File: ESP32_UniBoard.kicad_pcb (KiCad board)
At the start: 2 copper layers, 30 x 43.8 mm, 21 parts, among them J1 USB_C_Receptacle_USB2.0, J2 Conn_01x06_Socket, J3 Hirose DF40C, SW1 SW_Push, SW2 SW_Push, U1 ESP32-S3-WROOM-1, U2 SPX3819M5-L-3-3

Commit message: Schematics and PCB updates
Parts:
- added C9: 100nF, Capacitor_SMD:C_0603_1608Metric_Pad1.08x0.95mm_HandSolder, F.Cu at (116.7, 79.8)
- added D3: RED, LED_SMD:LED_0603_1608Metric_Pad1.05x0.95mm_HandSolder, F.Cu at (132.6, 77.7)
- added D4: YL, LED_SMD:LED_0603_1608Metric_Pad1.05x0.95mm_HandSolder, F.Cu at (134.6, 77.7)
- added F1: Polyfuse, Fuse:Fuse_1206_3216Metric_Pad1.42x1.75mm_HandSolder, F.Cu at (117.0, 82.9)
- added R5: R, Resistor_SMD:R_0603_1608Metric_Pad0.98x0.95mm_HandSolder, F.Cu at (132.6, 74.3)
- added R6: R, Resistor_SMD:R_0603_1608Metric_Pad0.98x0.95mm_HandSolder, F.Cu at (134.6, 74.3)
- added U3: USBLC6-2SC6, Package_TO_SOT_SMD:SOT-23-6, F.Cu at (117.1, 77.3)
- D2: renamed from D1; value LED -> GRN
- moved J3 13.9 mm to (121.3, 74.1), turned to 0 degrees
- moved R1 10.7 mm to (108.6, 84.4), turned to 180 degrees
- moved R2 4.93 mm to (112.1, 84.4), turned to 0 degrees
- moved C8 4.80 mm to (122.7, 81.0), turned to -90 degrees
- moved C6 4.52 mm to (124.8, 76.8)
- moved U2 4.39 mm to (125.7, 81.0)
- moved C7 4.30 mm to (125.9, 83.5)
- moved D2 3.52 mm to (130.5, 77.7)
- moved R4 3.41 mm to (130.5, 74.3)
- moved D1 2.87 mm to (121.0, 81.0)
- moved C1 1.80 mm to (108.2, 60.6)
- moved R3 1.77 mm to (108.2, 57.3)
- moved C2 0.21 mm to (133.0, 90.7)
- moved C5 0.21 mm to (110.4, 90.7)
- moved SW1 0.21 mm to (126.9, 90.7)
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- renumbered D2 to D1
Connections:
- D1 pad 2: Net-(D2-A) (its old number) -> Net-(D1-A)
- J1 pad A4: Net-(D2-A) (its old number) -> VBUS
- J1 pad A9: Net-(D2-A) (its old number) -> VBUS
- J1 pad B4: Net-(D2-A) (its old number) -> VBUS
- J1 pad B9: Net-(D2-A) (its old number) -> VBUS
- J3 pad 10: /GPIO17 -> /GPIO6
- J3 pad 11: /GPIO18 -> /GPIO5
- J3 pad 12: /GPIO8 -> /GPIO4
- J3 pad 14: /USB_D_N -> /GPIO1
- J3 pad 15: /USB_D_P -> /GPIO2
- J3 pad 16: /GPIO3 -> /ESP_TX
- J3 pad 17: /GPIO46 -> /ESP_RX
- J3 pad 19: /GPIO9 -> /GPIO42
- J3 pad 20: /GPIO10 -> /GPIO41
- J3 pad 21: /GPIO11 -> /GPIO40
- J3 pad 22: /GPIO12 -> /GPIO39
- J3 pad 23: /GPIO13 -> /GPIO38
- J3 pad 28: /GPIO14 -> unconnected-(J3-Pin_28-Pad28)
- J3 pad 29: /GPIO21 -> unconnected-(J3-Pin_29-Pad29)
- J3 pad 3: /GPIO4 -> /GPIO8
- J3 pad 30: /GPIO47 -> unconnected-(J3-Pin_30-Pad30)
- J3 pad 31: /GPIO48 -> unconnected-(J3-Pin_31-Pad31)
- J3 pad 32: /GPIO45 -> unconnected-(J3-Pin_32-Pad32)
- J3 pad 34: /BOOT -> unconnected-(J3-Pin_34-Pad34)
- J3 pad 35: /GPIO35 -> unconnected-(J3-Pin_35-Pad35)
- J3 pad 36: /GPIO36 -> unconnected-(J3-Pin_36-Pad36)
- J3 pad 37: /GPIO37 -> unconnected-(J3-Pin_37-Pad37)
- J3 pad 39: /GPIO38 -> unconnected-(J3-Pin_39-Pad39)
- J3 pad 4: /GPIO5 -> /GPIO18
- J3 pad 40: /GPIO39 -> /GPIO12
- J3 pad 41: /GPIO40 -> /GPIO11
- J3 pad 42: /GPIO41 -> /GPIO10
- J3 pad 44: /GPIO42 -> /GPIO9
- J3 pad 45: /ESP_RX -> /GPIO46
- J3 pad 46: /ESP_TX -> /GPIO3
- J3 pad 47: /GPIO2 -> /USB_D_N
- J3 pad 48: /GPIO1 -> /USB_D_P
- J3 pad 5: /GPIO6 -> /GPIO17
- J3 pad 6: /GPIO7 -> /GPIO16
- J3 pad 9: /GPIO16 -> /GPIO7
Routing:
- net /EN: track 7.25 -> 0.00 mm
- net +5V: track 7.24 -> 0.00 mm
- net Net-(J1-CC2): track 2.27 -> 0.00 mm
- net Net-(J1-CC1): track 2.16 -> 0.00 mm
- net +3V3: track 10.8 -> 8.66 mm
- net GND: track 3.16 -> 1.74 mm
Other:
- board text added: "IO35"
- board text added: "PWR"
- board text added: "RX"

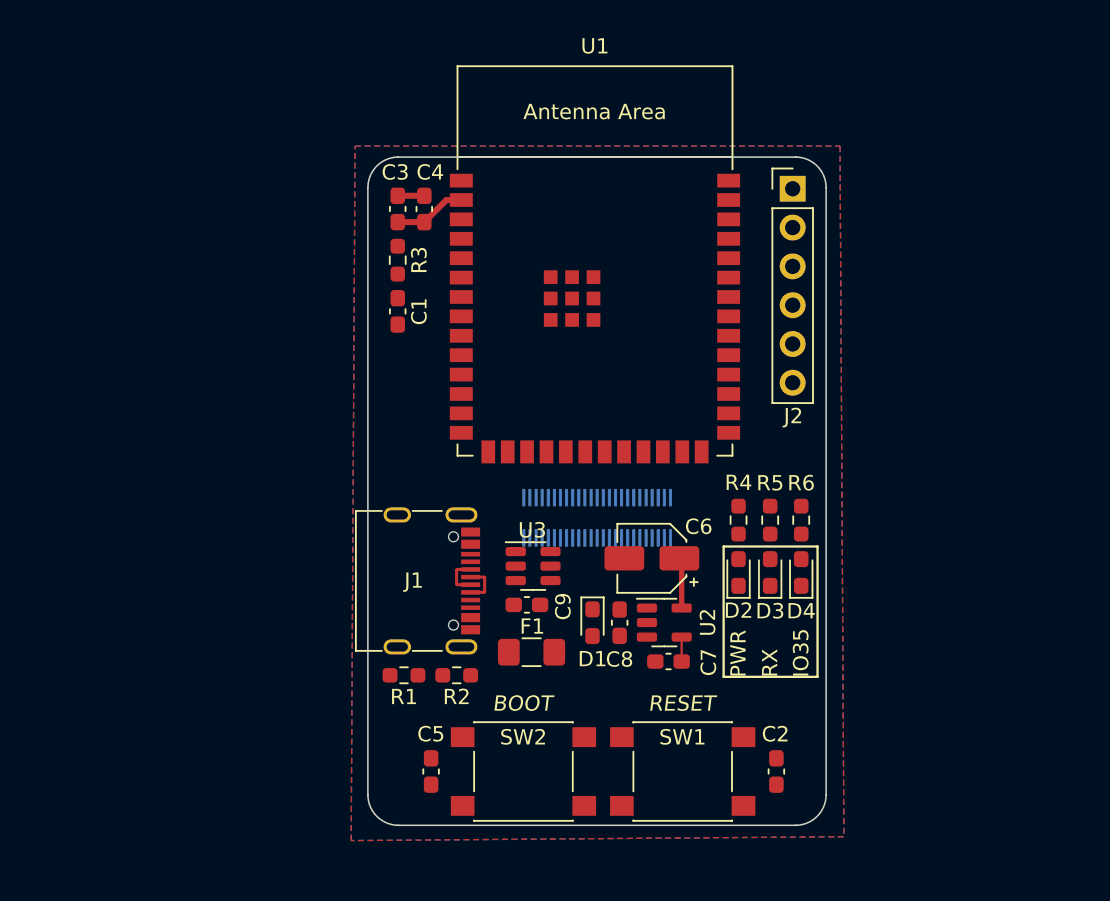
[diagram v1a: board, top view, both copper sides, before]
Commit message: Start of PCB routing
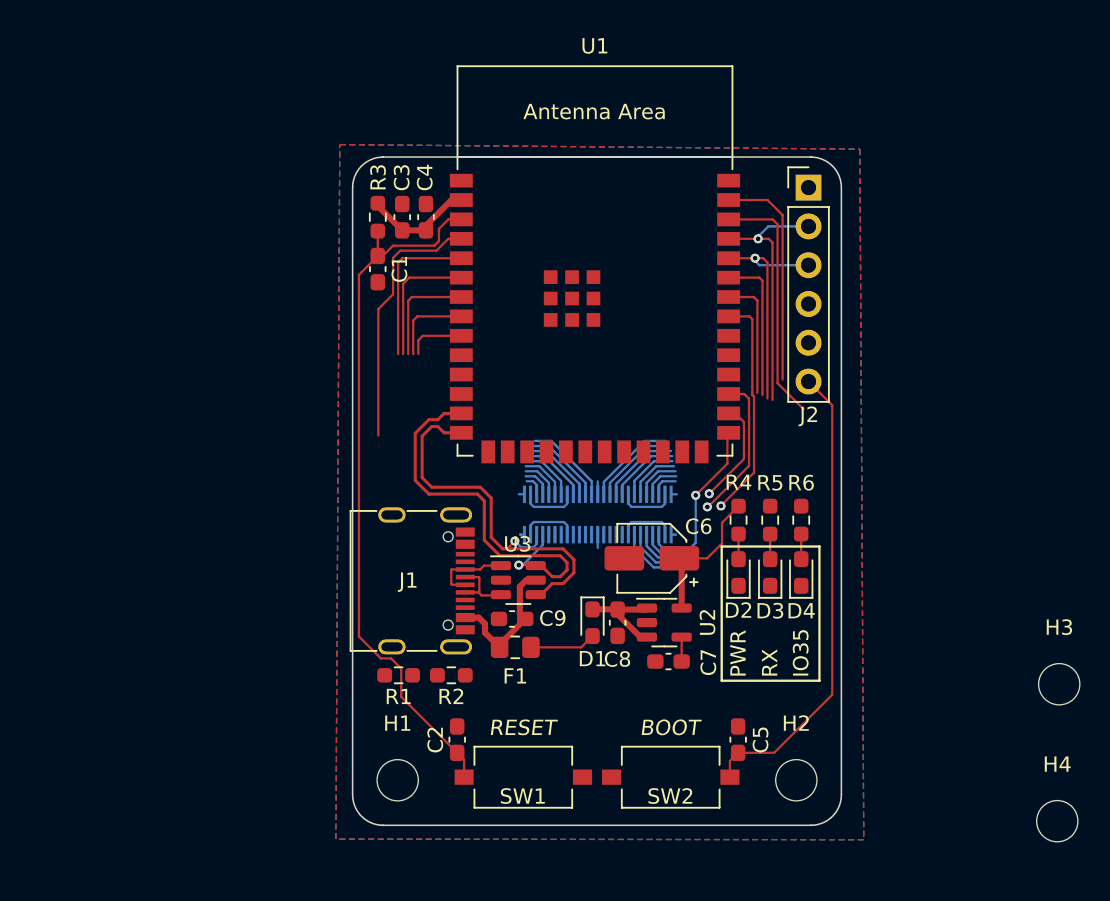
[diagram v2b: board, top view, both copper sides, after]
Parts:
- added H1: MountingHole, MountingHole:MountingHole_2.7mm_M2.5, F.Cu at (108.2, 91.3)
- added H2: MountingHole, MountingHole:MountingHole_2.7mm_M2.5, F.Cu at (134.3, 91.3)
- added H3: MountingHole, MountingHole:MountingHole_2.7mm_M2.5, F.Cu at (151.5, 85.0)
- added H4: MountingHole, MountingHole:MountingHole_2.7mm_M2.5, F.Cu at (151.4, 94.0)
- F1: footprint Fuse:Fuse_1206_3216Metric_Pad1.42x1.75mm_HandSolder -> Fuse:Fuse_0805_2012Metric_Pad1.15x1.40mm_HandSolder
- SW1, SW2: footprint Button_Switch_SMD:SW_SPST_PTS645 -> Button_Switch_SMD:SW_Tactile_SPST_NO_Straight_CK_PTS636Sx25SMTRLFS
- moved C2 21.0 mm to (112.1, 88.6), turned to -90 degrees
- moved C5 20.2 mm to (130.5, 88.6), turned to -90 degrees
- moved SW1 10.4 mm to (116.4, 91.1)
- moved SW2 9.65 mm to (126.1, 91.1), turned to 0 degrees
- moved R3 3.10 mm to (106.9, 54.4)
- moved C1 3.06 mm to (106.9, 57.8)
- moved U3 1.34 mm to (116.1, 78.2)
- moved C9 1.34 mm to (115.7, 80.7)
- moved F1 1.11 mm to (115.9, 82.6)
- moved J2 1.04 mm to (135.1, 52.5)
- moved C3 0.62 mm to (108.5, 54.4)
- moved C4 0.55 mm to (110.0, 54.4)
- moved R1 0.35 mm to (108.3, 84.4)
- moved R2 0.35 mm to (111.7, 84.4)
- moved J1 0.35 mm to (108.9, 78.2)
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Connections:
- J1 pad A6: /USB_D_P -> /D_P
- J1 pad A7: /USB_D_N -> /D_N
- J1 pad B6: /USB_D_P -> /D_P
- J1 pad B7: /USB_D_N -> /D_N
- J3 pad 28: unconnected-(J3-Pin_28-Pad28) -> /GPIO37
- J3 pad 29: unconnected-(J3-Pin_29-Pad29) -> /GPIO36
- J3 pad 30: unconnected-(J3-Pin_30-Pad30) -> /GPIO35
- J3 pad 31: unconnected-(J3-Pin_31-Pad31) -> /BOOT
- J3 pad 32: unconnected-(J3-Pin_32-Pad32) -> /GPIO45
- J3 pad 34: unconnected-(J3-Pin_34-Pad34) -> /GPIO48
- J3 pad 35: unconnected-(J3-Pin_35-Pad35) -> /GPIO47
- J3 pad 36: unconnected-(J3-Pin_36-Pad36) -> /GPIO21
- J3 pad 37: unconnected-(J3-Pin_37-Pad37) -> /GPIO14
- J3 pad 39: unconnected-(J3-Pin_39-Pad39) -> /GPIO13
- J3 pad 47: /USB_D_N -> /DPr_N
- J3 pad 48: /USB_D_P -> /DPr_P
- U1 pad 13: /USB_D_N -> /DPr_N
- U1 pad 14: /USB_D_P -> /DPr_P
- U3 pad 1: /USB_D_N -> /D_N
- U3 pad 3: /USB_D_P -> /D_P
- U3 pad 4: /USB_D_P -> /DPr_P
- U3 pad 6: /USB_D_N -> /DPr_N
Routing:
- net /EN: track 0.00 -> 46.4 mm
- net /BOOT: track 0.00 -> 44.2 mm, vias 0 -> 1
- net /DPr_N: track 0.00 -> 27.3 mm, vias 0 -> 1
- net /DPr_P: track 0.00 -> 26.3 mm, vias 0 -> 1
- net /GPIO4: track 0.00 -> 22.7 mm
- net /ESP_TX: track 0.00 -> 22.2 mm, vias 0 -> 1
- net /GPIO2: track 0.00 -> 21.7 mm
- net /GPIO1: track 0.00 -> 20.7 mm
- net /ESP_RX: track 0.00 -> 20.0 mm, vias 0 -> 1
- net /GPIO40: track 0.00 -> 17.8 mm, vias 0 -> 1
- net +3V3: track 8.66 -> 24.5 mm
- net /GPIO5: track 0.00 -> 15.5 mm
- net +5V: track 0.00 -> 14.1 mm
- net /GPIO42: track 0.00 -> 13.7 mm
- net /GPIO6: track 0.00 -> 13.3 mm
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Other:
- board size 30 x 43.8 mm -> 32 x 43.8 mm

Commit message: PCB rework
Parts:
- removed C7: 100nF, Capacitor_SMD:C_0603_1608Metric_Pad1.08x0.95mm_HandSolder
- moved H1 44.1 mm to (105.1, 47.3)
- moved H2 44.1 mm to (137.1, 47.3)
- moved J3 14.6 mm to (121.1, 88.5)
- moved C5 7.58 mm to (127.5, 95.6), turned to 0 degrees
- moved C2 7.20 mm to (113.8, 95.6), turned to 180 degrees
- moved SW1 2.97 mm to (113.8, 92.5)
- moved D1 2.86 mm to (120.7, 83.8)
- moved C8 2.85 mm to (122.4, 83.8)
- moved U2 2.85 mm to (125.6, 83.8)
- moved C6 2.75 mm to (124.6, 79.5)
- moved SW2 2.02 mm to (127.5, 92.5)
- moved D2 1.85 mm to (131.9, 78.9)
- moved D3 1.85 mm to (134.0, 78.9)
- moved D4 1.85 mm to (136.1, 78.9)
- moved R4 1.85 mm to (131.9, 75.4)
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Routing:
- net /BOOT: track 44.2 -> 34.4 mm, vias 1 -> 0
- net /GPIO17: track 2.58 -> 12.4 mm, vias 0 -> 1
- net Net-(J1-CC1): track 0.00 -> 9.35 mm
- net /GPIO40: track 17.8 -> 8.42 mm, vias 1 -> 0
- net /GPIO36: track 12.0 -> 3.38 mm, vias 1 -> 0
- net /GPIO6: track 13.3 -> 21.8 mm, vias 0 -> 1
- net /GPIO7: track 11.6 -> 19.9 mm, vias 0 -> 1
- net /GPIO16: track 6.99 -> 15.1 mm, vias 0 -> 1
- net /GPIO15: track 9.19 -> 17.1 mm, vias 0 -> 1
- net /GPIO48: track 0.00 -> 7.75 mm, vias 0 -> 1
- net VBUS: track 9.44 -> 16.9 mm, vias 0 -> 2
- net +3V3: track 24.5 -> 17.5 mm
- net /EN: track 46.4 -> 53.5 mm
- net Net-(J1-CC2): track 0.00 -> 6.36 mm
- net /GPIO35: track 9.72 -> 3.95 mm, vias 1 -> 0
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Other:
- board size 32 x 43.8 mm -> 33.5 x 46.1 mm

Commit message: Routing complete
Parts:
- removed H4: MountingHole, MountingHole:MountingHole_2.7mm_M2.5
- added C7: 100nF, Capacitor_SMD:C_0603_1608Metric_Pad1.08x0.95mm_HandSolder, F.Cu at (128.6, 83.8)
- added REF**: KiCad-Logo2_5mm_SilkScreen, Symbol:KiCad-Logo2_5mm_SilkScreen, B.Cu at (133.1, 87.3)
- moved H3 31.6 mm to (121.1, 93.6)
- moved C5 4.10 mm to (131.6, 95.4)
- moved SW2 4.10 mm to (131.6, 92.3)
- moved C2 3.19 mm to (110.6, 95.5)
- moved SW1 3.19 mm to (110.6, 92.3)
- moved H1 2.00 mm to (107.1, 47.3)
- moved H2 2.00 mm to (135.1, 47.3)
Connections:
- J3 pad 10: /GPIO6 -> /GPIO10
- J3 pad 11: /GPIO5 -> /GPIO11
- J3 pad 12: /GPIO4 -> /GPIO12
- J3 pad 14: /GPIO1 -> /GPIO13
- J3 pad 15: /GPIO2 -> /GPIO14
- J3 pad 16: /ESP_TX -> /GPIO21
- J3 pad 17: /ESP_RX -> /GPIO47
- J3 pad 19: /GPIO42 -> /GPIO48
- J3 pad 20: /GPIO41 -> /GPIO45
- J3 pad 21: /GPIO40 -> /BOOT
- J3 pad 22: /GPIO39 -> /GPIO35
- J3 pad 23: /GPIO38 -> /GPIO36
- J3 pad 29: /GPIO36 -> /GPIO38
- J3 pad 30: /GPIO35 -> /GPIO39
- J3 pad 31: /BOOT -> /GPIO40
- J3 pad 32: /GPIO45 -> /GPIO41
- J3 pad 34: /GPIO48 -> /GPIO42
- J3 pad 35: /GPIO47 -> /ESP_RX
- J3 pad 36: /GPIO21 -> /ESP_TX
- J3 pad 37: /GPIO14 -> /GPIO2
- J3 pad 39: /GPIO13 -> /GPIO1
- J3 pad 4: /GPIO18 -> /DPr_P
- J3 pad 40: /GPIO12 -> /GPIO4
- J3 pad 41: /GPIO11 -> /GPIO5
- J3 pad 42: /GPIO10 -> /GPIO6
- J3 pad 44: /GPIO9 -> /GPIO7
- J3 pad 45: /GPIO46 -> /GPIO15
- J3 pad 46: /GPIO3 -> /GPIO16
- J3 pad 47: /DPr_N -> /GPIO17
- J3 pad 48: /DPr_P -> /GPIO18
- J3 pad 5: /GPIO17 -> /DPr_N
- J3 pad 6: /GPIO16 -> /GPIO3
- J3 pad 7: /GPIO15 -> /GPIO46
- J3 pad 9: /GPIO7 -> /GPIO9
- R6 pad 1: /GPIO35 -> /GPIO1
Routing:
- net +3V3: track 17.5 -> 99.7 mm, vias 0 -> 5
- net /ESP_RX: track 16.3 -> 71.2 mm
- net /GPIO1: track 18.2 -> 59.5 mm, vias 0 -> 2
- net /ESP_TX: track 18.2 -> 55.1 mm
- net /GPIO2: track 16.6 -> 52.2 mm, vias 0 -> 1
- net /EN: track 53.5 -> 87.8 mm, vias 0 -> 2
- net /GPIO42: track 11.6 -> 44.6 mm, vias 0 -> 1
- net /GPIO41: track 10.0 -> 41.9 mm, vias 0 -> 1
- net /GPIO40: track 8.42 -> 39.4 mm, vias 0 -> 1
- net /GPIO4: track 22.5 -> 53.0 mm
- net /GPIO39: track 6.78 -> 36.9 mm, vias 0 -> 1
- net /GPIO38: track 5.06 -> 34.4 mm, vias 0 -> 1
- net /BOOT: track 34.4 -> 63.1 mm, vias 0 -> 2
- net /GPIO5: track 20.2 -> 48.7 mm
- net /GPIO8: track 0.00 -> 25.3 mm, vias 0 -> 1
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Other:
- board size 33.5 x 46.1 mm -> 34 x 52.3 mm
- board text added: "3V3"
- board text added: "ESP32 UniBoard"
- board text added: "GND"
- board text added: "IO1"
- board text added: "RST"
- board text added: "TX"
- board text added: "V1.0"
- board text removed: "IO35"

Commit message: Adjustments in Schematic and PCB
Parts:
- removed REF**: KiCad-Logo2_5mm_SilkScreen, Symbol:KiCad-Logo2_5mm_SilkScreen
- C2, C5: value 100n -> 100nF
- moved J1 0.69 mm to (107.9, 79.6)
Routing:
- net +5V: track 24.5 -> 27.1 mm
- net GND: track 15.6 -> 13.2 mm, vias 72 -> 82
- net /D_N: track 5.36 -> 6.13 mm
- net /D_P: track 4.49 -> 5.12 mm
- net /GPIO4: track 53.0 -> 53.6 mm

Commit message: -
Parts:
- J3: footprint Hirose_Connector_DF40C:Hirose_DF40C-50 -> Hirose_Connector_DF40C:Hirose_DF40C-50DS
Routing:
- net +5V: track 27.1 -> 26.5 mm

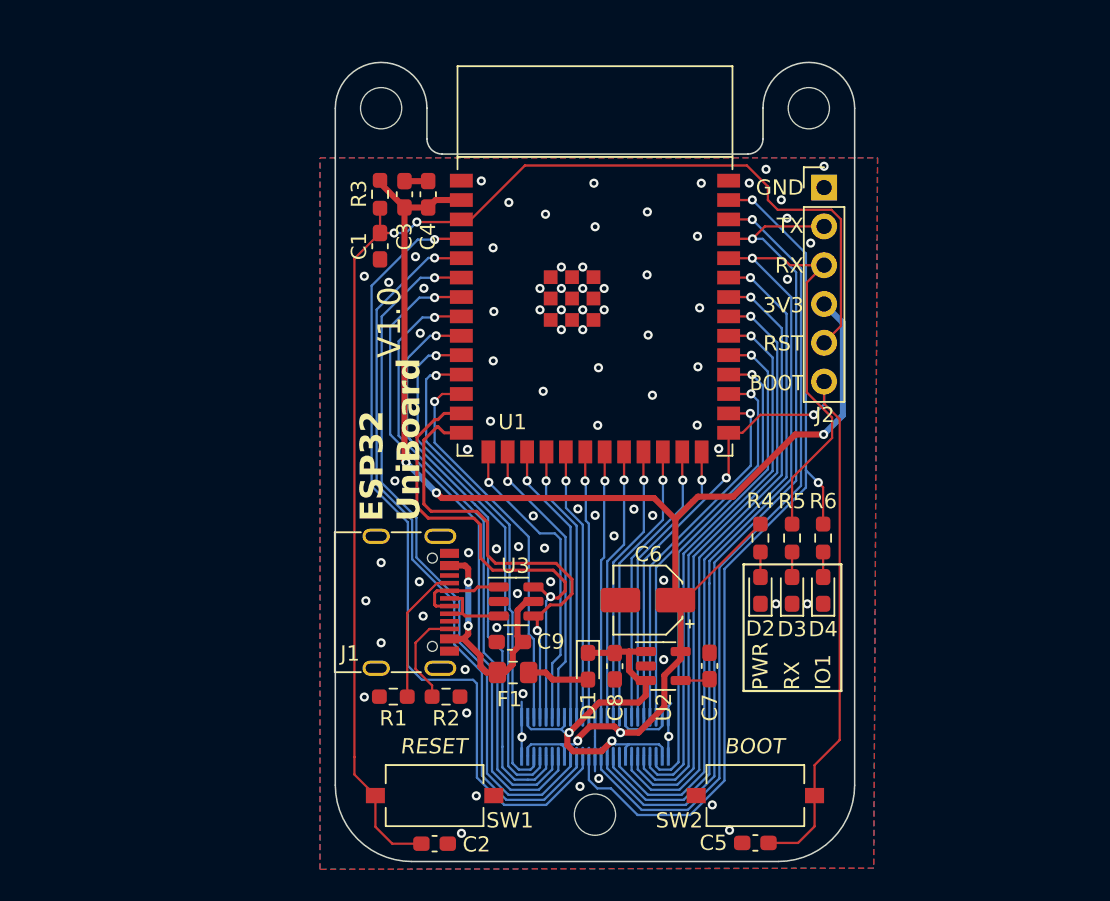
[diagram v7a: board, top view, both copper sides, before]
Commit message: PCB changed to 4 Layer WIP
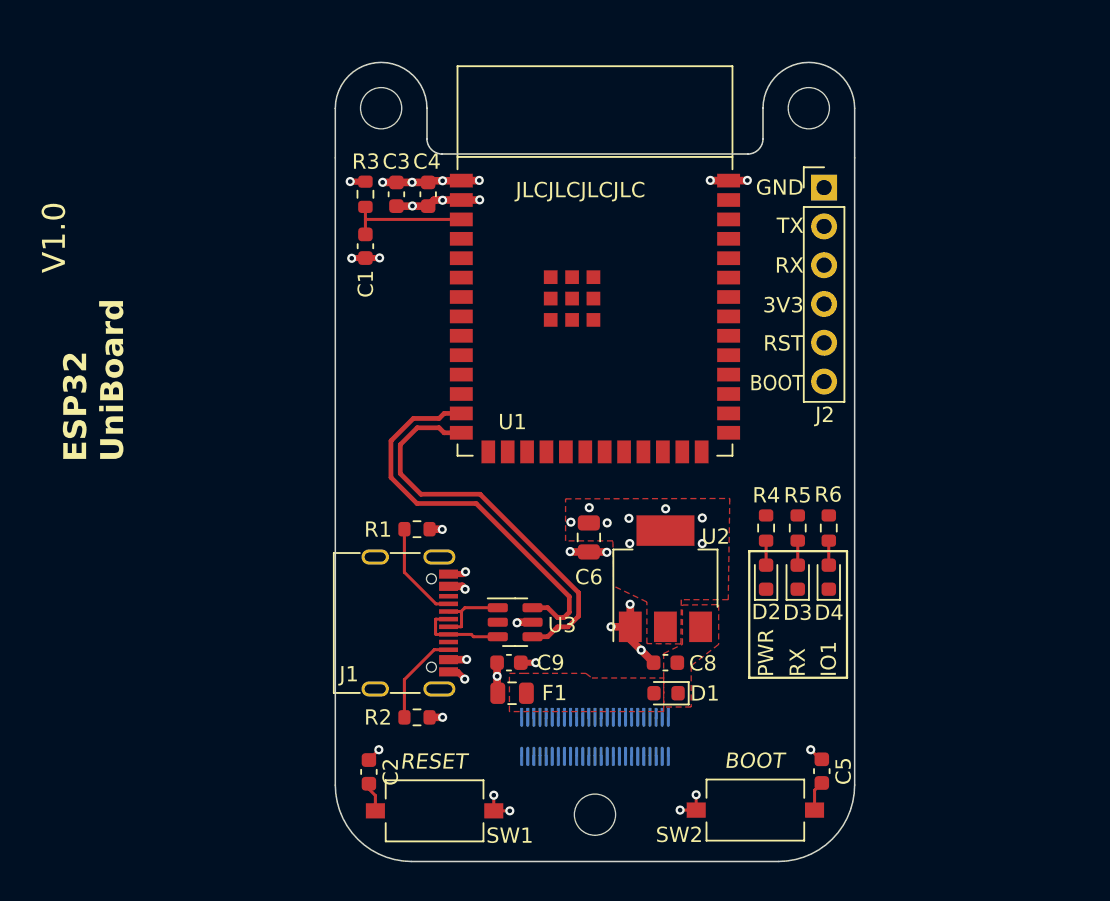
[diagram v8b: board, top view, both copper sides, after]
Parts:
- removed C7: 100nF, Capacitor_SMD:C_0603_1608Metric_Pad1.08x0.95mm_HandSolder
- C1, C2, C3, C4, C5, C9: footprint Capacitor_SMD:C_0603_1608Metric_Pad1.08x0.95mm_HandSolder -> Capacitor_SMD:C_0603_1608Metric
- C6: value 2u2F -> 22uF; footprint Capacitor_SMD:CP_Elec_4x5.4 -> Capacitor_SMD:C_0805_2012Metric
- C8: value 1uF -> 10uF; footprint Capacitor_SMD:C_0603_1608Metric_Pad1.08x0.95mm_HandSolder -> Capacitor_SMD:C_0603_1608Metric
- D1: footprint Diode_SMD:D_0603_1608Metric_Pad1.05x0.95mm_HandSolder -> Diode_SMD:D_0603_1608Metric
- D2, D3, D4: footprint LED_SMD:LED_0603_1608Metric_Pad1.05x0.95mm_HandSolder -> LED_SMD:LED_0603_1608Metric
- F1: footprint Fuse:Fuse_0805_2012Metric_Pad1.15x1.40mm_HandSolder -> Fuse:Fuse_0805_2012Metric
- R1, R2, R3, R4, R5, R6: footprint Resistor_SMD:R_0603_1608Metric_Pad0.98x0.95mm_HandSolder -> Resistor_SMD:R_0603_1608Metric
- U2: value SPX3819M5-L-3-3 -> AZ1117-3.3; footprint Package_TO_SOT_SMD:SOT-23-5 -> Package_TO_SOT_SMD:SOT-223-3_TabPin2
- moved R1 11.1 mm to (109.5, 74.9), turned to 0 degrees
- moved C5 6.40 mm to (136.0, 90.7), turned to -90 degrees
- moved C2 6.37 mm to (106.3, 90.8), turned to -90 degrees
- moved U2 5.72 mm to (125.7, 78.1), turned to 90 degrees
- moved C6 5.63 mm to (120.7, 75.4), turned to -90 degrees
- moved D1 5.40 mm to (125.8, 85.6), turned to 180 degrees
- moved C8 3.33 mm to (125.7, 83.6), turned to 180 degrees
- moved R2 2.34 mm to (109.5, 87.2)
- moved F1 1.36 mm to (115.7, 85.6)
- moved C9 1.36 mm to (115.5, 83.6), turned to 0 degrees
- moved J1 1.36 mm to (107.8, 81.0)
- moved U3 1.36 mm to (115.9, 81.0)
- moved SW1 1.00 mm to (110.6, 93.3)
- moved C1 0.96 mm to (106.1, 56.3)
- moved R3 0.96 mm to (106.1, 52.9)
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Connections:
- net Net-(D1-A) renamed /VBUS_Fused
- net Net-(J1-CC1) renamed /R_CC1
- net Net-(J1-CC2) renamed /R_CC2
- U2 pad 1: +5V -> GND
- U2 pad 2: GND -> +3V3
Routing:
- net +3V3: track 99.7 -> 6.66 mm, vias 5 -> 12
- net /EN: track 87.8 -> 10.0 mm, vias 2 -> 0
- net /ESP_RX: track 71.2 -> 0.00 mm, vias 1 -> 0
- net /BOOT: track 63.1 -> 1.97 mm, vias 2 -> 0
- net /GPIO1: track 59.5 -> 0.00 mm, vias 2 -> 0
- net /ESP_TX: track 55.1 -> 0.00 mm, vias 1 -> 0
- net /GPIO4: track 53.6 -> 0.00 mm, vias 1 -> 0
- net /GPIO2: track 52.2 -> 0.00 mm, vias 1 -> 0
- net /GPIO5: track 48.7 -> 0.00 mm, vias 1 -> 0
- net /GPIO6: track 46.5 -> 0.00 mm, vias 1 -> 0
- net /GPIO42: track 44.6 -> 0.00 mm, vias 1 -> 0
- net /GPIO7: track 43.6 -> 0.00 mm, vias 1 -> 0
- net /GPIO41: track 41.9 -> 0.00 mm, vias 1 -> 0
- net /GPIO15: track 40.7 -> 0.00 mm, vias 1 -> 0
- net /GPIO40: track 39.4 -> 0.00 mm, vias 1 -> 0
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- added copper zone on F.Cu, net +3V3
- added copper zone on In2.Cu, net +3V3
- added copper zone on F.Cu, net +5V
- added copper zone on F.Cu, net /VBUS_Fused
- added copper zone on In1.Cu, net GND
- added copper zone on In2.Cu, net VBUS
- removed copper zone on B.Cu, net GND
- removed copper zone on F.Cu, net GND
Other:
- copper layers 2 -> 4
- board text added: "JLCJLCJLCJLC"
